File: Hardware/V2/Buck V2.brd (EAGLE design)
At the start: 77.5 x 50.2 mm, 54 parts, among them Q1 IRF3205STRLPBF, Q2 IRF3205STRLPBF, Q3 IRF3205STRLPBF, Q4 IRF3205STRLPBF, U1 Value

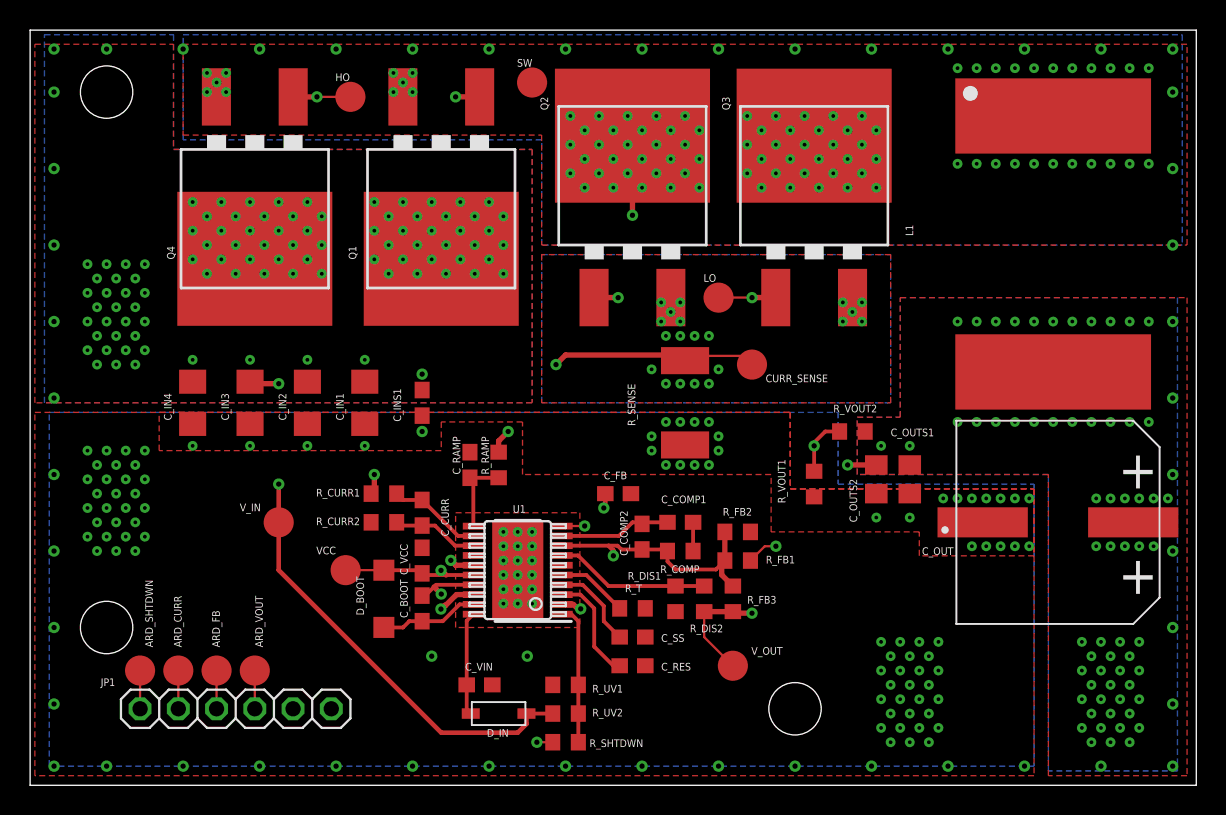
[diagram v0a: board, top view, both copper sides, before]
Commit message: updated buck v2.1 to reflect actual boards ordered from JLC
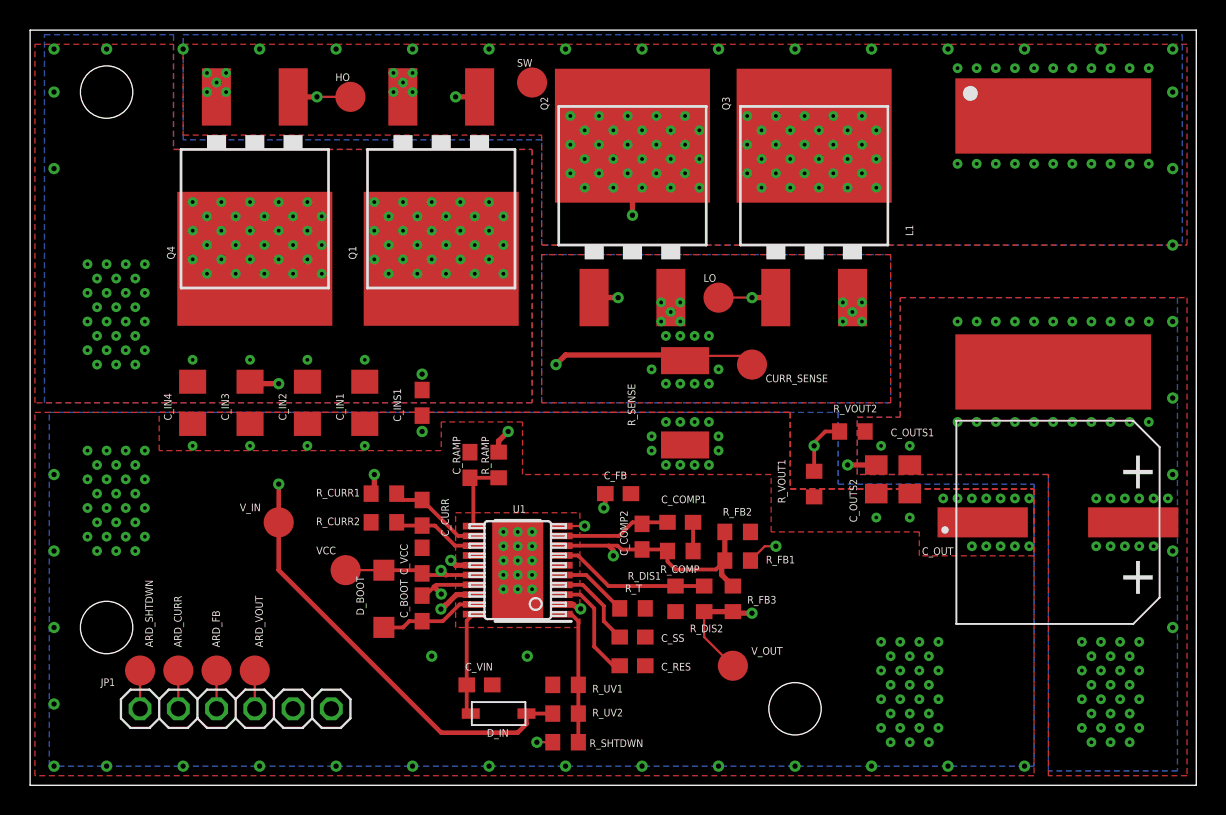
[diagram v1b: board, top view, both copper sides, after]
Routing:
- net N$7: track 38.2 -> 38.8 mm
